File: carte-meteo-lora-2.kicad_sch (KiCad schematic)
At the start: 80 parts, among them J1 USB_C_Receptacle_USB2.0_14P, J4 Conn_01x04_Pin, J6 Conn_Coaxial, J7 Conn_Coaxial, J8 Conn_Coaxial, SW1 SW_Push, SW2 SW_Push, U3 HS96L03W2C03, U4 LDL212PV33R, U6 ESP32-C5, U8 SX1262TR8-GC, Y1 48M

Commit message: schem: assign footprints
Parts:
- C16, C17: footprint (none) -> Capacitor_SMD:C_0402_1005Metric
- J6, J7, J8: footprint (none) -> Connector_Coaxial:SMA_BAT_Wireless_BWSMA-KWE-Z001
- L3, L4: footprint (none) -> Inductor_SMD:L_0402_1005Metric
- R5, R6, R7, R8: footprint (none) -> Resistor_SMD:R_0402_1005Metric
- TP1, TP2, TP3, TP4, TP5, TP6, TP7, TP8, TP9: footprint (none) -> GLCS:Murata_MM8930-2620
- U8: footprint (none) -> GLCS:Silicontra_SX1262ZTR8
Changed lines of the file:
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@@
 			)
 		)
-		(property "Footprint" ""
+		(property "Footprint" "Connector_Coaxial:SMA_BAT_Wireless_BWSMA-KWE-Z001"
 			(at 78.74 175.26 0)
 			(hide yes)
@@
 			)
 		)
-		(property "Footprint" ""
+		(property "Footprint" "Capacitor_SMD:C_0402_1005Metric"
 			(at 81.5848 68.58 0)
 			(hide yes)
@@
 			)
 		)
-		(property "Footprint" ""
+		(property "Footprint" "Inductor_SMD:L_0402_1005Metric"
 			(at 91.44 64.77 0)
 			(hide yes)
@@
 			)
 		)
-		(property "Footprint" ""
+		(property "Footprint" "GLCS:Murata_MM8930-2620"
 			(at 100.33 111.76 0)
 			(hide yes)
@@
 			)
 		)
-		(property "Footprint" ""
+		(property "Footprint" "GLCS:Murata_MM8930-2620"
 			(at 109.22 130.81 0)
 			(hide yes)
@@
 			)
 		)
-		(property "Footprint" ""
+		(property "Footprint" "Inductor_SMD:L_0402_1005Metric"
 			(at 91.44 34.29 0)
 			(hide yes)
@@
 			)
 		)
-		(property "Footprint" ""
+		(property "Footprint" "Resistor_SMD:R_0402_1005Metric"
 			(at 113.538 116.84 90)
 			(hide yes)
@@
 			)
 		)
-		(property "Footprint" ""
+		(property "Footprint" "GLCS:Murata_MM8930-2620"
 			(at 88.9 100.33 0)
 			(hide yes)
@@
 			)
 		)
-		(property "Footprint" ""
+		(property "Footprint" "Resistor_SMD:R_0402_1005Metric"
 			(at 113.792 116.84 90)
 			(hide yes)
@@
 			)
 		)
-		(property "Footprint" ""
+		(property "Footprint" "GLCS:Murata_MM8930-2620"
 			(at 73.66 64.77 0)
 			(hide yes)
@@
 			)
 		)
-		(property "Footprint" ""
+		(property "Footprint" "Capacitor_SMD:C_0402_1005Metric"
 			(at 101.2952 68.58 0)
 			(hide yes)
@@
 			)
 		)
-		(property "Footprint" ""
+		(property "Footprint" "GLCS:Murata_MM8930-2620"
 			(at 73.66 34.29 0)
 			(hide yes)
@@
 			)
 		)
-		(property "Footprint" ""
+		(property "Footprint" "Connector_Coaxial:SMA_BAT_Wireless_BWSMA-KWE-Z001"
 			(at 57.15 64.77 0)
 			(hide yes)
@@
 			)
 		)
-		(property "Footprint" ""
+		(property "Footprint" "GLCS:Silicontra_SX1262ZTR8"
 			(at 96.52 182.88 0)
 			(hide yes)
@@
 			)
 		)
-		(property "Footprint" ""
+		(property "Footprint" "GLCS:Murata_MM8930-2620"
 			(at 92.71 130.81 0)
 			(hide yes)
@@
 			)
 		)
-		(property "Footprint" ""
+		(property "Footprint" "GLCS:Murata_MM8930-2620"
 			(at 109.22 100.33 0)
 			(hide yes)
@@
 			)
 		)
-		(property "Footprint" ""
+		(property "Footprint" "Resistor_SMD:R_0402_1005Metric"
 			(at 84.328 116.84 90)
 			(hide yes)
@@
 			)
 		)
-		(property "Footprint" ""
+		(property "Footprint" "Connector_Coaxial:SMA_BAT_Wireless_BWSMA-KWE-Z001"
 			(at 57.15 34.29 0)
 			(hide yes)
@@
 			)
 		)
-		(property "Footprint" ""
+		(property "Footprint" "GLCS:Murata_MM8930-2620"
 			(at 110.49 64.77 0)
 			(hide yes)
@@
 			)
 		)
-		(property "Footprint" ""
+		(property "Footprint" "Resistor_SMD:R_0402_1005Metric"
 			(at 84.582 116.84 90)
 			(hide yes)
@@
 			)
 		)
-		(property "Footprint" ""
+		(property "Footprint" "GLCS:Murata_MM8930-2620"
 			(at 110.49 34.29 0)
 			(hide yes)

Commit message: schem: add title
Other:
- company: (none) -> Rémi Ait-Younes
- title: (none) -> Carte Meteo Lora 2
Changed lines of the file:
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@@
 	(generator_version "10.0")
 	(paper "A4")
+	(title_block
+		(title "Carte Meteo Lora 2")
+		(date "2026-05-26")
+		(rev "01")
+		(company "Rémi Ait-Younes")
+	)
 	(rectangle
 		(start 250.19 58.42)

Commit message: schem: add ordering info to BOM
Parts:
- C16, C17: Basic (none) -> X; JLCPCB Part # (none) -> C76910; Manufacturer (none) -> muRata; Manufacturer Part Number (none) -> GJM1555C1HR40BB01D
- J6, J7, J8: Basic (none) -> Z; JLCPCB Part # (none) -> C496551; Manufacturer (none) -> BAT WIRELESS; Manufacturer Part Number (none) -> BWSMA-KWE-Z001
- L4: Basic (none) -> X; JLCPCB Part # (none) -> C162539; Manufacturer (none) -> muRata; Manufacturer Part Number (none) -> LQG15HS1N6S02D
- R5, R6, R7, R8: Basic (none) -> Y; JLCPCB Part # (none) -> C25076; Manufacturer (none) -> Uniroyal Elec; Manufacturer Part Number (none) -> 0402WGF1000TCE
- TP1, TP2, TP3, TP4, TP5, TP6, TP7, TP8, TP9: Basic (none) -> X; JLCPCB Part # (none) -> C6227587; Manufacturer (none) -> muRata; Manufacturer Part Number (none) -> MM8930-2620RJ4
- U3: Basic (none) -> Z; JLCPCB Part # (none) -> C5248080; Manufacturer (none) -> HS; Manufacturer Part Number (none) -> HS96L03W2C03; now in the parts list
- U6: Manufacturer (none) -> Espressif; Manufacturer Part Number (none) -> ESP32-C5HF4

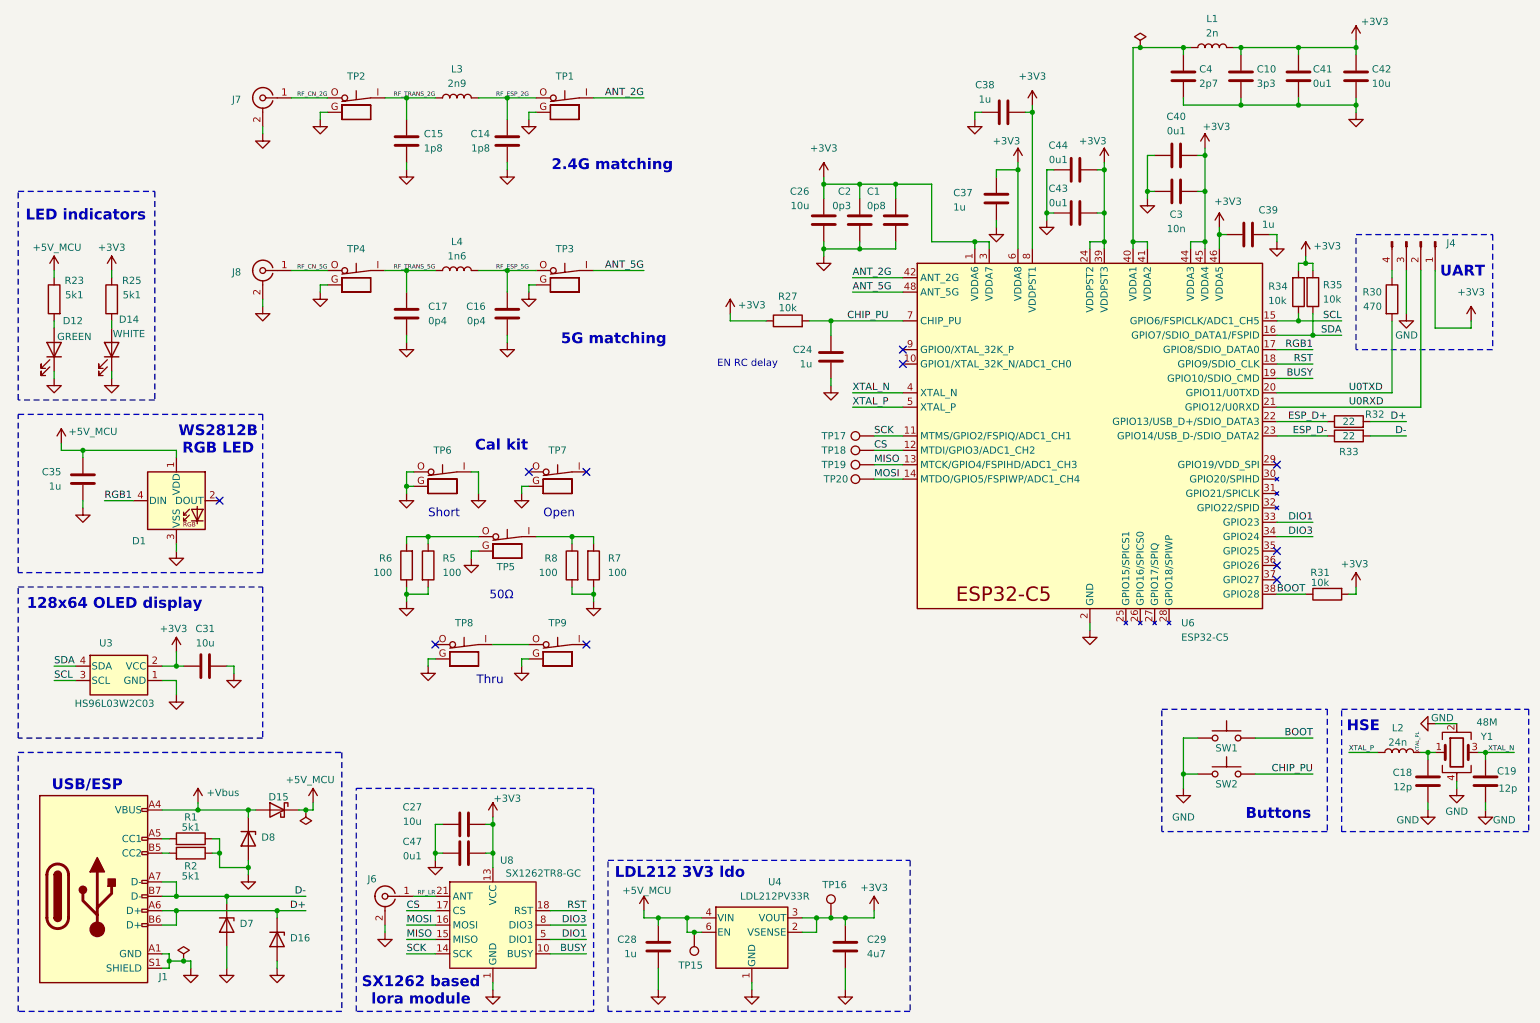
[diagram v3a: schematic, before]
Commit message: schem: renumber
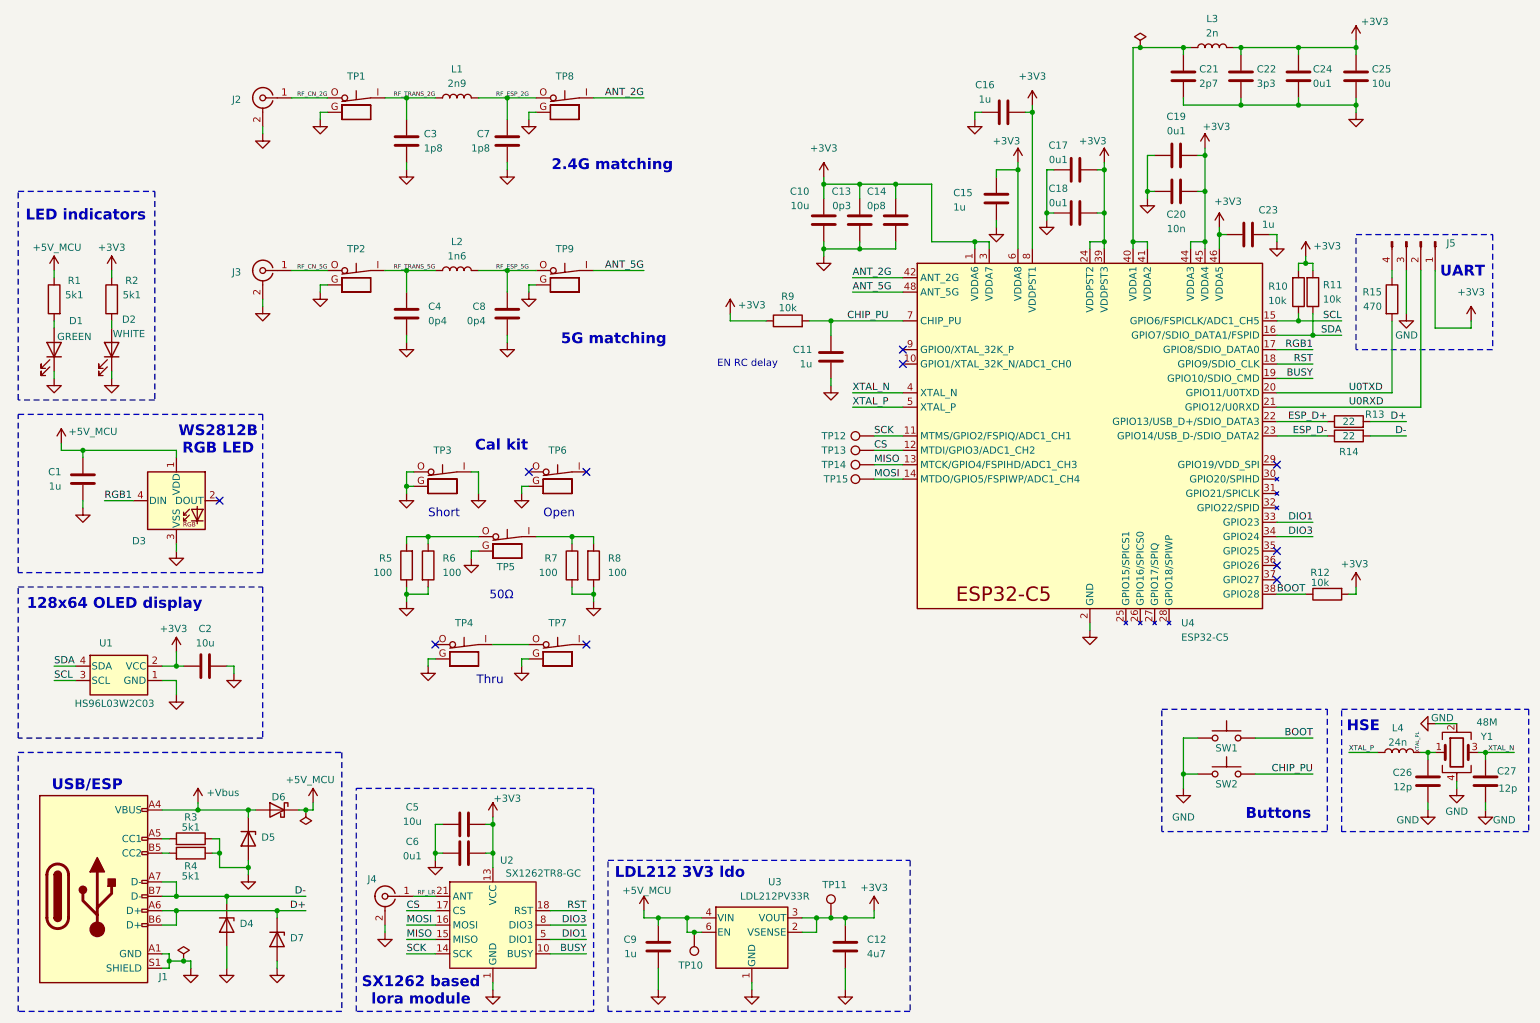
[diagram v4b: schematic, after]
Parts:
- renumbered C35 to C1, C26 to C10, C24 to C11, C29 to C12, C2 to C13, C1 to C14, C37 to C15, C38 to C16, C44 to C17, C43 to C18, C40 to C19, C31 to C2, C3 to C20, C4 to C21, C10 to C22, C39 to C23, C41 to C24, C42 to C25, C18 to C26, C19 to C27, C15 to C3, C17 to C4, C27 to C5, C47 to C6, C14 to C7, C16 to C8, C28 to C9, D12 to D1, D14 to D2, D1 to D3, D7 to D4, D8 to D5, D15 to D6, D16 to D7, J7 to J2, J8 to J3, J6 to J4, J4 to J5, L3 to L1, L4 to L2, L1 to L3, L2 to L4, R23 to R1, R34 to R10, R35 to R11, R31 to R12, R32 to R13, R33 to R14, R30 to R15, R25 to R2, R1 to R3, R2 to R4, R6 to R5, R5 to R6, R8 to R7, R7 to R8, R27 to R9, TP2 to TP1, TP15 to TP10, TP16 to TP11, TP17 to TP12, TP18 to TP13, TP19 to TP14, TP20 to TP15, TP4 to TP2, TP6 to TP3, TP8 to TP4, TP7 to TP6, TP9 to TP7, TP1 to TP8, TP3 to TP9, U3 to U1, U8 to U2, U4 to U3, U6 to U4

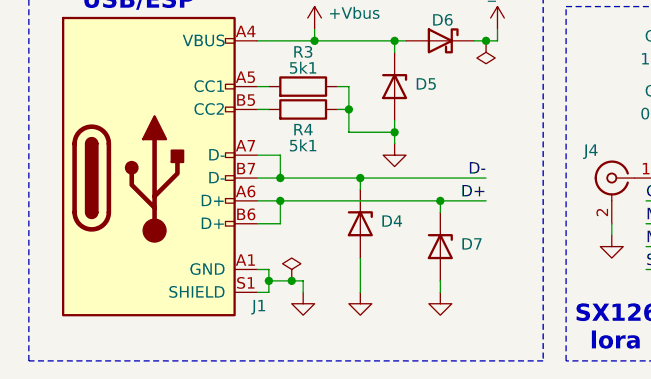
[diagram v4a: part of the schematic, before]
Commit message: pcb: import footprints from schem
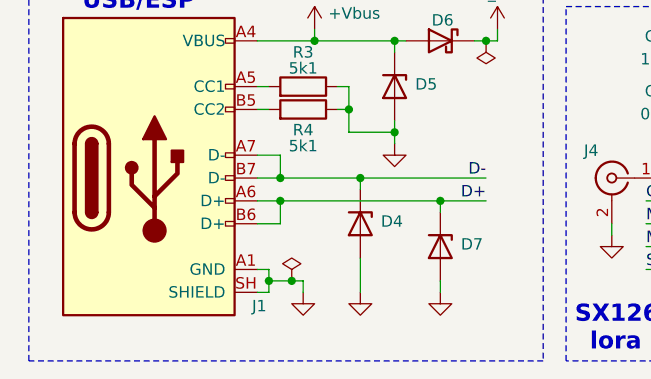
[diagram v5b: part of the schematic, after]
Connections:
- net GND: now also J1.SH (SHIELD); no longer J1.S1 (SHIELD)
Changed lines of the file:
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@@
 		(pin "A1"
 		)
-		(pin "S1"
+		(pin "SH"
 		)
 		(pin "B9"

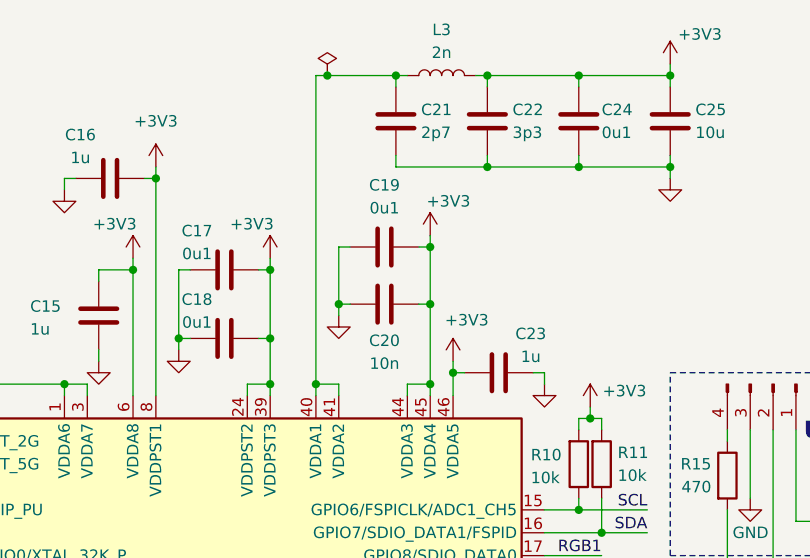
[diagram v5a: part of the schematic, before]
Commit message: pcb: initial section
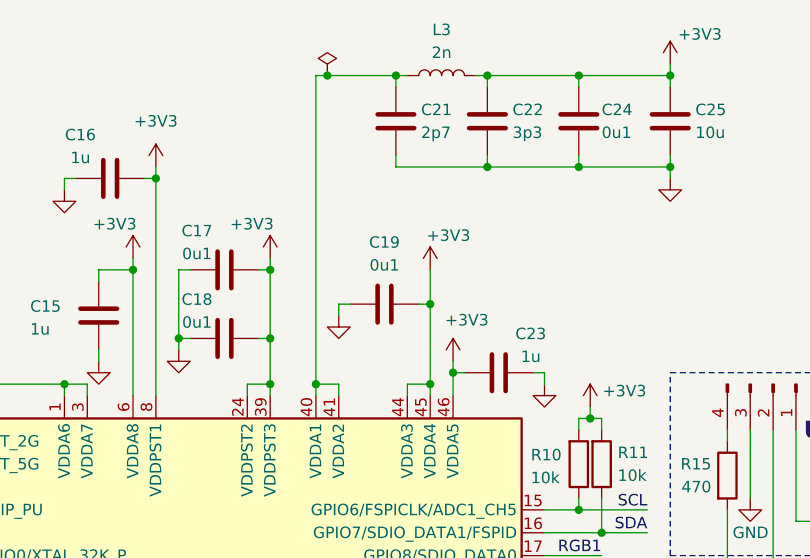
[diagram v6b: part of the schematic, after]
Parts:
- removed C20: 10n, Capacitor_SMD:C_0402_1005Metric, symbol Device:C
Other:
- moved on the sheet: C19
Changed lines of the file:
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@@
 	)
 	(junction
-		(at 223.52 50.8)
-		(diameter 0)
-		(color 0 0 0 0)
-	)
-	(junction
 		(at 212.09 25.4)
 		(diameter 0)
@@
 	)
 	(junction
-		(at 223.52 44.45)
-		(diameter 0)
-		(color 0 0 0 0)
-	)
-	(junction
 		(at 82.55 121.92)
 		(diameter 0)
@@
 	)
 	(junction
-		(at 87.63 167.64)
+		(at 223.52 50.8)
 		(diameter 0)
 		(color 0 0 0 0)
 	)
 	(junction
-		(at 100.33 64.77)
+		(at 87.63 167.64)
 		(diameter 0)
 		(color 0 0 0 0)
 	)
 	(junction
-		(at 213.36 50.8)
+		(at 100.33 64.77)
 		(diameter 0)
 		(color 0 0 0 0)
@@
 	(wire
 		(pts
-			(xy 213.36 50.8) (xy 213.36 44.45)
-		)
-		(stroke
-			(width 0)
-			(type default)
-		)
-	)
-	(wire
-		(pts
 			(xy 67.31 68.58) (xy 67.31 67.31)
 		)
@@
 	(wire
 		(pts
-			(xy 222.25 44.45) (xy 223.52 44.45)
-		)
-		(stroke
-			(width 0)
-			(type default)
-		)
-	)
-	(wire
-		(pts
 			(xy 82.55 111.76) (xy 82.55 113.03)
 		)
@@
 	(wire
 		(pts
-			(xy 223.52 44.45) (xy 223.52 50.8)
+			(xy 223.52 46.99) (xy 223.52 50.8)
 		)
 		(stroke
@@
 	(wire
 		(pts
-			(xy 223.52 43.18) (xy 223.52 44.45)
-		)
-		(stroke
-			(width 0)
-			(type default)
-		)
-	)
-	(wire
-		(pts
 			(xy 54.61 168.91) (xy 54.61 170.18)
 		)
@@
 	(wire
 		(pts
-			(xy 213.36 44.45) (xy 214.63 44.45)
-		)
-		(stroke
-			(width 0)
-			(type default)
-		)
-	)
-	(wire
-		(pts
 			(xy 139.7 73.66) (xy 146.05 73.66)
 		)
@@
 	(symbol
 		(lib_id "power:+3V3")
-		(at 223.52 43.18 0)
+		(at 223.52 46.99 0)
 		(mirror y)
 		(unit 1)
@@
 		(dnp no)
 		(property "Reference" "#PWR057"
-			(at 223.52 46.99 0)
+			(at 223.52 50.8 0)
 			(hide yes)
 			(show_name no)
@@
 		)
 		(property "Value" "+3V3"
-			(at 225.552 39.37 0)
+			(at 225.552 43.18 0)
 			(show_name no)
 			(do_not_autoplace no)
@@
 		)
 		(property "Footprint" ""
-			(at 223.52 43.18 0)
+			(at 223.52 46.99 0)
 			(hide yes)
 			(show_name no)
@@
 		)
 		(property "Datasheet" ""
-			(at 223.52 43.18 0)
+			(at 223.52 46.99 0)
 			(hide yes)
 			(show_name no)
@@
 		)
 		(property "Description" "Power symbol creates a global label with name \"+3V3\""
-			(at 223.52 43.18 0)
+			(at 223.52 46.99 0)
 			(hide yes)
 			(show_name no)
@@
 	)
 	(symbol
-		(lib_id "Device:C")
-		(at 218.44 50.8 270)
-		(mirror x)
-		(unit 1)
-		(body_style 1)
-		(exclude_from_sim no)
-		(in_bom yes)
-		(on_board yes)
-		(in_pos_files yes)
-		(dnp no)
-		(property "Reference" "C20"
-			(at 218.44 54.864 90)
-			(show_name no)
-			(do_not_autoplace no)
-			(effects
-				(font
-					(size 1.27 1.27)
-				)
-			)
-		)
-		(property "Value" "10n"
-			(at 218.44 57.404 90)
-			(show_name no)
-			(do_not_autoplace no)
-			(effects
-				(font
-					(size 1.27 1.27)
-				)
-			)
-		)
-		(property "Footprint" "Capacitor_SMD:C_0402_1005Metric"
-			(at 214.63 49.8348 0)
-			(hide yes)
-			(show_name no)
-			(do_not_autoplace no)
-			(effects
-				(font
-					(size 1.27 1.27)
-				)
-			)
-		)
-		(property "Datasheet" ""
-			(at 218.44 50.8 0)
-			(hide yes)
-			(show_name no)
-			(do_not_autoplace no)
-			(effects
-				(font
-					(size 1.27 1.27)
-				)
-			)
-		)
-		(property "Description" "Unpolarized capacitor"
-			(at 218.44 50.8 0)
-			(hide yes)
-			(show_name no)
-			(do_not_autoplace no)
-			(effects
-				(font
-					(size 1.27 1.27)
-				)
-			)
-		)
-		(property "Basic" "Y"
-			(at 218.44 50.8 90)
-			(hide yes)
-			(show_name no)
-			(do_not_autoplace no)
-			(effects
-				(font
-					(size 1.27 1.27)
-				)
-			)
-		)
-		(property "JLCPCB Part #" "C15195"
-			(at 218.44 50.8 90)
-			(hide yes)
-			(show_name no)
-			(do_not_autoplace no)
-			(effects
-				(font
-					(size 1.27 1.27)
-				)
-			)
-		)
-		(property "Manufacturer" "Samsung Electro-Mechanics "
-			(at 218.44 50.8 90)
-			(hide yes)
-			(show_name no)
-			(do_not_autoplace no)
-			(effects
-				(font
-					(size 1.27 1.27)
-				)
-			)
-		)
-		(property "Manufacturer Part Number" "CL05B103KB5NNNC"
-			(at 218.44 50.8 90)
-			(hide yes)
-			(show_name no)
-			(do_not_autoplace no)
-			(effects
-				(font
-					(size 1.27 1.27)
-				)
-			)
-		)
-		(pin "1"
-		)
-		(pin "2"
-		)
-		(instances
-			(project "carte-meteo-lora-2"
-				(path "/14cd50fe-ec77-4829-bd74-9322c036cdc1"
-					(reference "C20")
-					(unit 1)
-				)
-			)
-		)
-	)
-	(symbol
 		(lib_id "power:+3V3")
 		(at 226.06 57.15 0)
@@
 	(symbol
 		(lib_id "Device:C")
-		(at 218.44 44.45 270)
+		(at 218.44 50.8 270)
 		(mirror x)
 		(unit 1)
@@
 		(dnp no)
 		(property "Reference" "C19"
-			(at 218.44 37.592 90)
+			(at 218.44 43.942 90)
 			(show_name no)
 			(do_not_autoplace no)
@@
 		)
 		(property "Value" "0u1"
-			(at 218.44 40.132 90)
+			(at 218.44 46.482 90)
 			(show_name no)
 			(do_not_autoplace no)
@@
 		)
 		(property "Footprint" "Capacitor_SMD:C_0402_1005Metric"
-			(at 214.63 43.4848 0)
+			(at 214.63 49.8348 0)
 			(hide yes)
 			(show_name no)
@@
 		)
 		(property "Datasheet" ""
-			(at 218.44 44.45 0)
+			(at 218.44 50.8 0)
 			(hide yes)
 			(show_name no)
@@
 		)
 		(property "Description" "Unpolarized capacitor"
-			(at 218.44 44.45 0)
+			(at 218.44 50.8 0)
 			(hide yes)
 			(show_name no)
@@
 		)
 		(property "Manufacturer" "Samsung Electro-Mechanics "
-			(at 218.44 44.45 0)
+			(at 218.44 50.8 0)
 			(hide yes)
 			(show_name no)
@@
 		)
 		(property "Manufacturer Part Number" "CL05B104KB54PNC"
-			(at 218.44 44.45 0)
+			(at 218.44 50.8 0)
 			(hide yes)
 			(show_name no)
@@
 		)
 		(property "Basic" "Y"
-			(at 218.44 44.45 0)
+			(at 218.44 50.8 0)
 			(hide yes)
 			(show_name no)
@@
 		)
 		(property "JLCPCB Part #" "C307331"
-			(at 218.44 44.45 0)
+			(at 218.44 50.8 0)
 			(hide yes)
 			(show_name no)

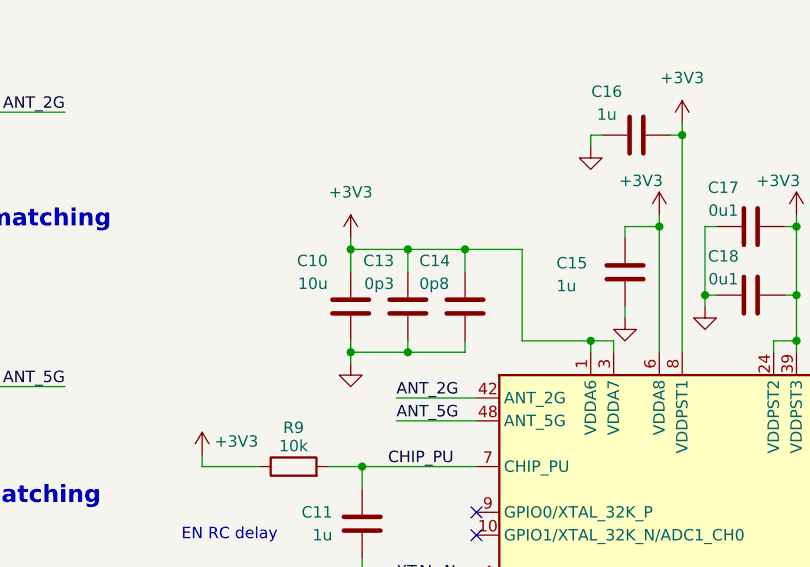
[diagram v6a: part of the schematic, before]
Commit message: pcb: add edge cut
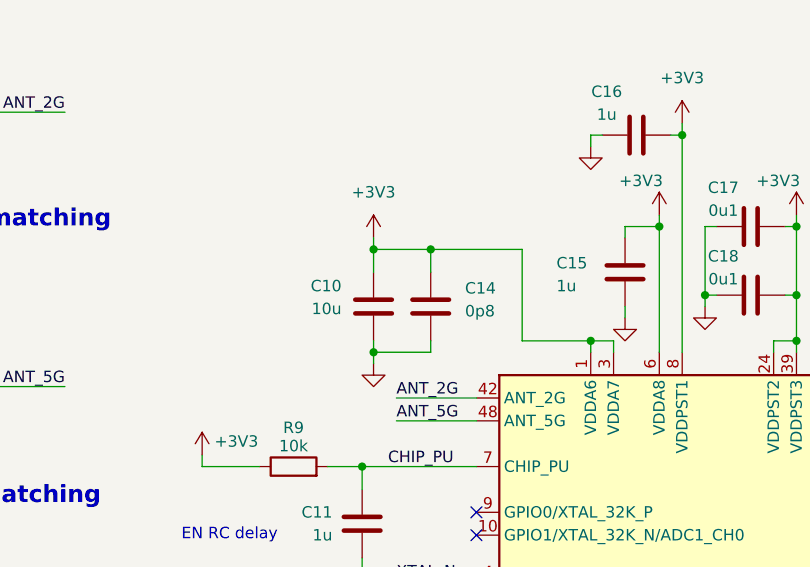
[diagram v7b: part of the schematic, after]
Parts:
- removed C13: 0p3, Capacitor_SMD:C_0402_1005Metric, symbol Device:C
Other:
- moved on the sheet: C10, C14

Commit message: pcb: add m2 mouting holes
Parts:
- added H1, H2: MountingHole_Pad, MountingHole:MountingHole_2.2mm_M2_Pad_Via, symbol Mechanical:MountingHole_Pad
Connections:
- net GND: now also H1.1, H2.1
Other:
- note added: "Mounting"
